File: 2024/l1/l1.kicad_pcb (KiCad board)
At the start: 2 copper layers, 175 x 169.4 mm, 72 parts, among them J1 Conn_01x04, J2 Conn_01x02, SW1 SW_SPDT, U2 CD74HC4067M, U3 TPS5430DDA, U4 TPS5430DDA

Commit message: final 0.9
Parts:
- added J3: Conn_01x02, Connector_AMASS:AMASS_XT60-M_1x02_P7.20mm_Vertical, F.Cu at (31.2, 99.2)
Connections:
- net /RX renamed /RXL2
- net /TX renamed /TXL2
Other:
- outline, holes or cut-outs redrawn

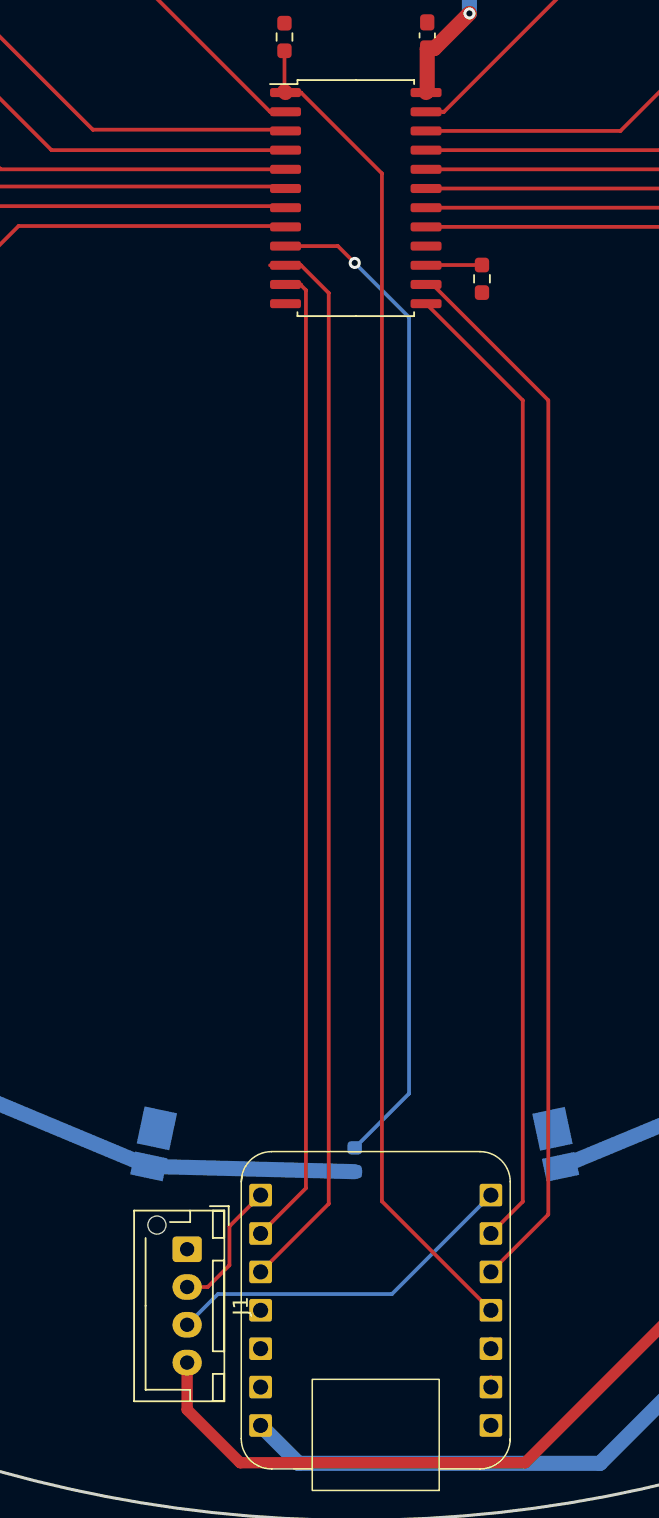
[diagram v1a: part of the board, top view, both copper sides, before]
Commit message: final 0.91
fixed:
switched analog signal pin on l1 esp32c3 to a0 since a1 not working
silkscreen is now properly placed
traces are adjusted on l1
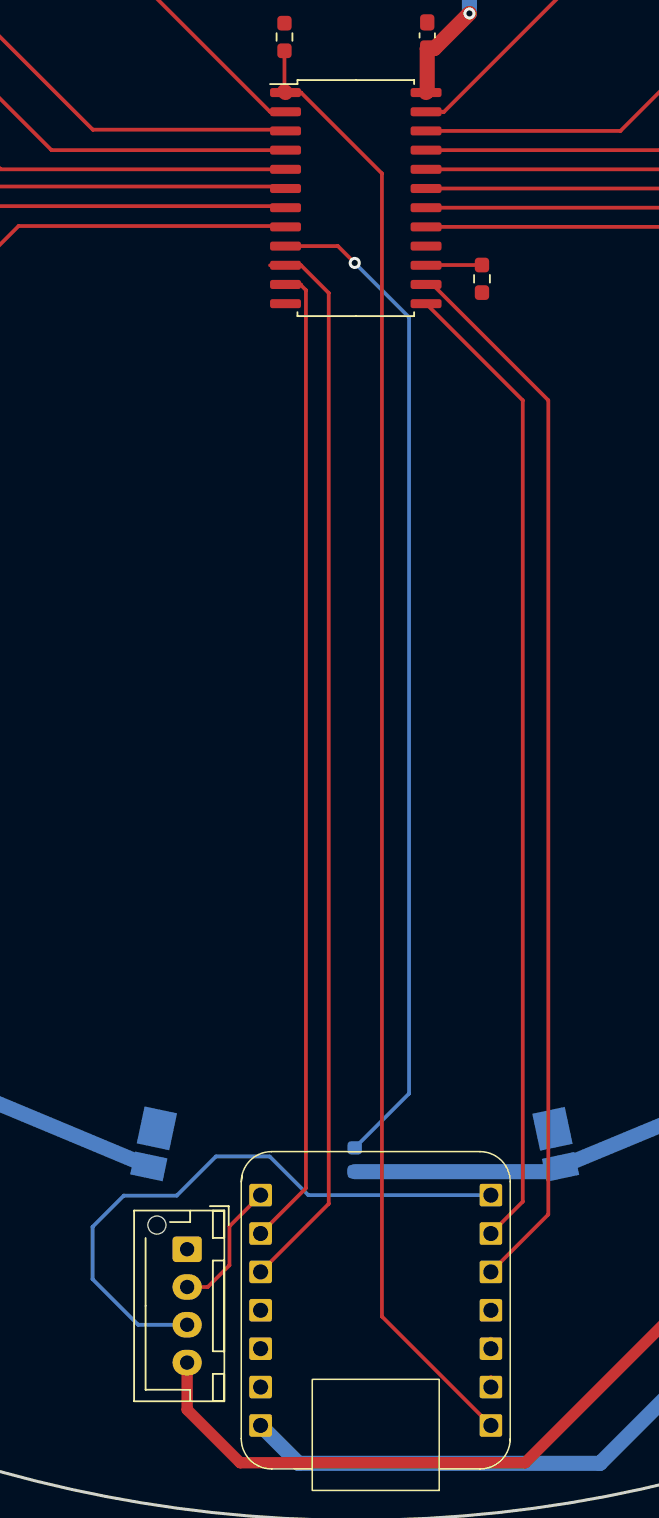
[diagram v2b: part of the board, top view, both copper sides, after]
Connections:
- U1 pad 0: unconnected-(U1-D0-Pad0) -> /M1
- U1 pad 3: /M1 -> unconnected-(U1-D3-Pad3)
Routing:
- net /TXL2: track 23.7 -> 40.3 mm
- net /M1: track 89.6 -> 97.5 mm
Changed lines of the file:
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@@
 	(net 57 "unconnected-(U3-NC-Pad3)")
 	(net 58 "unconnected-(U3-EN-Pad5)")
-	(net 59 "unconnected-(U1-D0-Pad0)")
+	(net 59 "unconnected-(U1-D3-Pad3)")
 	(net 60 "unconnected-(U1-D1-Pad1)")
 	(net 61 "unconnected-(U1-D2-Pad2)")
@@
 			(at 3.75 -3.55 -90)
 			(layer "F.SilkS")
+			(hide yes)
 			(effects
 				(font
@@
 			(remove_unused_layers no)
 			(roundrect_rratio 0.1)
-			(net 59 "unconnected-(U1-D0-Pad0)")
+			(net 18 "/M1")
 			(pinfunction "D0")
 			(pintype "bidirectional")
@@
 			(remove_unused_layers no)
 			(roundrect_rratio 0.1)
-			(net 18 "/M1")
+			(net 59 "unconnected-(U1-D3-Pad3)")
 			(pinfunction "D3")
 			(pintype "bidirectional")
@@
 	)
 	(segment
-		(start 91.303226 169.077528)
-		(end 104.93 169.4275)
-		(width 1)
-		(layer "B.Cu")
-		(net 1)
-	)
-	(segment
 		(start 39.826113 110.668579)
 		(end 39.826113 111.774639)
@@
 	)
 	(segment
+		(start 118.231268 169.4275)
+		(end 118.550053 169.108715)
+		(width 1)
+		(layer "B.Cu")
+		(net 1)
+	)
+	(segment
 		(start 78.417097 45.109429)
 		(end 67.187097 52.835913)
@@
 	)
 	(segment
+		(start 104.93 169.4275)
+		(end 118.231268 169.4275)
+		(width 1)
+		(layer "B.Cu")
+		(net 1)
+	)
+	(segment
 		(start 80.931738 104.231853)
 		(end 100.306738 104.231853)
@@
 	)
 	(segment
-		(start 106.73 103.37)
+		(start 101.375 98.015)
+		(end 106.73 103.37)
+		(width 0.25)
+		(layer "F.Cu")
+		(net 18)
+	)
+	(segment
+		(start 100.35 98.015)
 		(end 101.375 98.015)
 		(width 0.25)
@@
 	)
 	(segment
-		(start 100.28 95.25)
-		(end 100.28 97.945)
+		(start 106.73 103.37)
+		(end 106.73 179.01)
 		(width 0.25)
 		(layer "F.Cu")
@@
 	)
 	(segment
-		(start 113.94 178.6)
-		(end 106.73 171.39)
+		(start 100.28 95.25)
+		(end 100.28 97.945)
 		(width 0.25)
 		(layer "F.Cu")
@@
 	)
 	(segment
-		(start 106.73 171.39)
-		(end 106.73 103.37)
+		(start 106.73 179.01)
+		(end 113.94 186.22)
 		(width 0.25)
 		(layer "F.Cu")
@@
 	)
 	(segment
-		(start 101.375 98.015)
-		(end 100.35 98.015)
+		(start 113.64 186.22)
+		(end 113.94 186.22)
 		(width 0.25)
 		(layer "F.Cu")
@@
 	)
 	(segment
-		(start 113.64 186.22)
-		(end 113.94 186.22)
-		(width 0.25)
-		(layer "F.Cu")
-		(net 59)
-	)
-	(segment
 		(start 113.94 183.011752)
 		(end 113.94 183.68)
@@
 	)
 	(segment
-		(start 93.84 179.56)
-		(end 95.875 177.525)
+		(start 87.58 176.54)
+		(end 90.6 179.56)
+		(width 0.25)
+		(layer "B.Cu")
+		(net 191)
+	)
+	(segment
+		(start 89.65 171.01)
+		(end 87.58 173.08)
+		(width 0.25)
+		(layer "B.Cu")
+		(net 191)
+	)
+	(segment
+		(start 87.58 173.08)
+		(end 87.58 176.54)
+		(width 0.25)
+		(layer "B.Cu")
+		(net 191)
+	)
+	(segment
+		(start 90.6 179.56)
+		(end 93.84 179.56)
+		(width 0.25)
+		(layer "B.Cu")
+		(net 191)
+	)
+	(segment
+		(start 101.86 170.98)
+		(end 99.3 168.42)
+		(width 0.25)
+		(layer "B.Cu")
+		(net 191)
+	)
+	(segment
+		(start 95.74 168.42)
+		(end 93.15 171.01)
+		(width 0.25)
+		(layer "B.Cu")
+		(net 191)
+	)
+	(segment
+		(start 113.94 170.98)
+		(end 101.86 170.98)
 		(width 0.25)
 		(layer "B.Cu")
@@
 	)
 	(segment
-		(start 107.395 177.525)
-		(end 113.94 170.98)
+		(start 99.3 168.42)
+		(end 95.74 168.42)
 		(width 0.25)
 		(layer "B.Cu")
@@
 	)
 	(segment
-		(start 95.875 177.525)
-		(end 107.395 177.525)
+		(start 93.15 171.01)
+		(end 89.65 171.01)
 		(width 0.25)
 		(layer "B.Cu")
